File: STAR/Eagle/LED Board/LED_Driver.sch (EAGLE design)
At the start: 8 parts

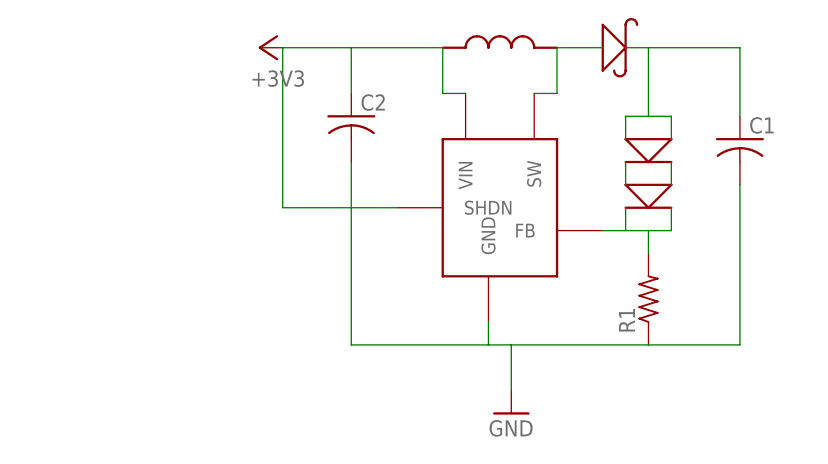
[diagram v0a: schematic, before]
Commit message: LED board, added text
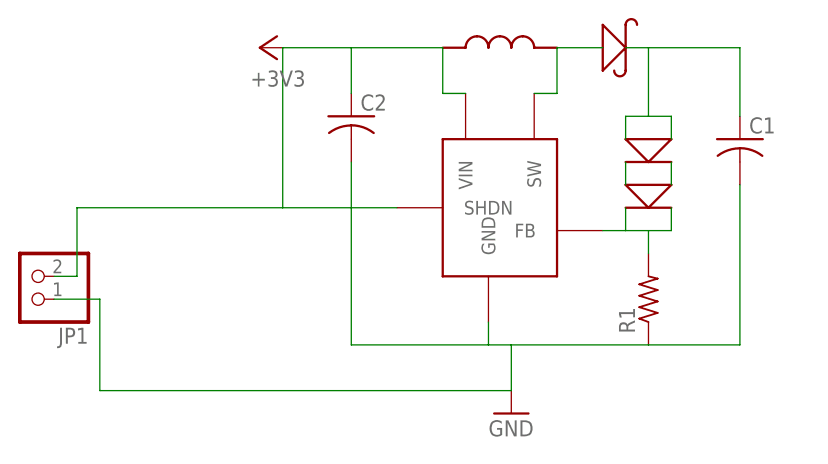
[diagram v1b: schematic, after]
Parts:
- added JP1: (no value), pinhead:PINHD-1X2
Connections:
- net +3V3: now also JP1.2
- net GND: now also JP1.1
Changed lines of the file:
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@@
 <layer number="98" name="Guide" color="6" fill="1" visible="yes" active="yes"/>
 <layer number="99" name="SpiceOrder" color="5" fill="1" visible="yes" active="yes"/>
+<layer number="200" name="200bmp" color="1" fill="10" visible="yes" active="yes"/>
 </layers>
 <schematic xreflabel="%F%N/%S.%C%R" xrefpart="/%S.%C%R">
@@
 <part name="C2" library="resistor" deviceset="C-US" device="C0603"/>
 <part name="GND1" library="supply1" deviceset="GND" device=""/>
+<part name="JP1" library="pinhead" deviceset="PINHD-1X2" device=""/>
 </parts>
 <sheets>
@@
 <instance part="C2" gate="G$1" x="58.42" y="71.12"/>
 <instance part="GND1" gate="1" x="76.2" y="38.1"/>
+<instance part="JP1" gate="G$1" x="22.86" y="53.34" rot="R180"/>
 </instances>
 <busses>
@@
 <wire x1="63.5" y1="60.96" x2="50.8" y2="60.96" width="0.1524" layer="91"/>
 <wire x1="50.8" y1="60.96" x2="50.8" y2="78.74" width="0.1524" layer="91"/>
+<wire x1="50.8" y1="60.96" x2="27.94" y2="60.96" width="0.1524" layer="91"/>
+<wire x1="27.94" y1="60.96" x2="27.94" y2="53.34" width="0.1524" layer="91"/>
+<pinref part="JP1" gate="G$1" pin="2"/>
+<wire x1="27.94" y1="53.34" x2="25.4" y2="53.34" width="0.1524" layer="91"/>
 </segment>
 </net>
@@
 <wire x1="76.2" y1="45.72" x2="76.2" y2="40.64" width="0.1524" layer="91"/>
 <pinref part="GND1" gate="1" pin="GND"/>
+<wire x1="76.2" y1="40.64" x2="30.48" y2="40.64" width="0.1524" layer="91"/>
+<wire x1="30.48" y1="40.64" x2="30.48" y2="50.8" width="0.1524" layer="91"/>
+<pinref part="JP1" gate="G$1" pin="1"/>
+<wire x1="30.48" y1="50.8" x2="25.4" y2="50.8" width="0.1524" layer="91"/>
 </segment>
 </net>

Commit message: screws
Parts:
- C1: value (none) -> .1uF
- C2: value (none) -> 22uF
- R1: value (none) -> 4.75
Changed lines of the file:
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@@
 <part name="U$4" library="LED" deviceset="CLA2A-WKW-CYBZ0343CT" device=""/>
 <part name="U$5" library="LED" deviceset="CLA2A-WKW-CYBZ0343CT" device=""/>
-<part name="R1" library="resistor" deviceset="R-US_" device="R0603"/>
-<part name="C1" library="resistor" deviceset="C-US" device="C0603"/>
+<part name="R1" library="resistor" deviceset="R-US_" device="R0603" value="4.75"/>
+<part name="C1" library="resistor" deviceset="C-US" device="C0603" value=".1uF"/>
 <part name="+3V1" library="supply1" deviceset="+3V3" device=""/>
-<part name="C2" library="resistor" deviceset="C-US" device="C0603"/>
+<part name="C2" library="resistor" deviceset="C-US" device="C0603" value="22uF"/>
 <part name="GND1" library="supply1" deviceset="GND" device=""/>
 <part name="JP1" library="pinhead" deviceset="PINHD-1X2" device=""/>
